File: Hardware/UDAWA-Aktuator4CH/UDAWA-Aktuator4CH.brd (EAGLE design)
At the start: 100 x 80 mm, 23 parts

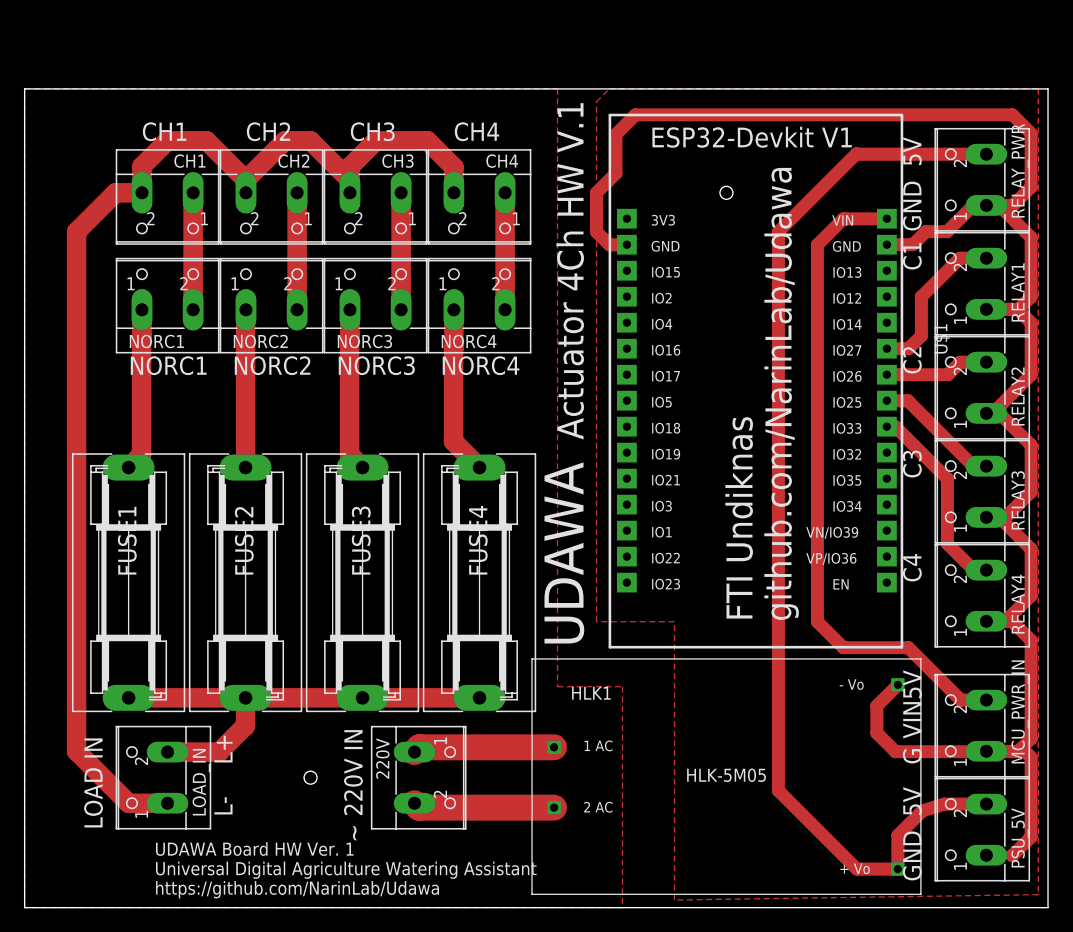
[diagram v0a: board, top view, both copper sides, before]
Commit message: Revisi mirroring. Board tidak mirror. Silkscreen mirror.
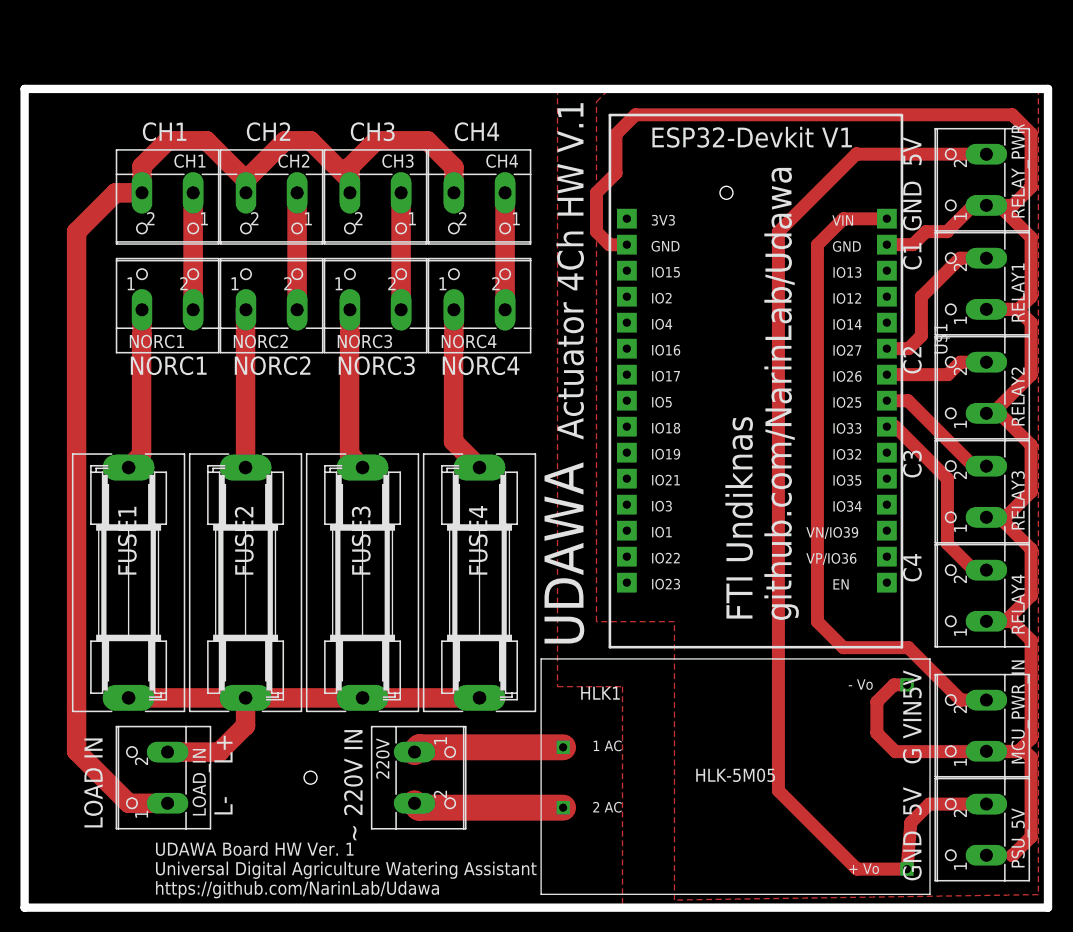
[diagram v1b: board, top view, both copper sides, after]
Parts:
- moved HLK1 0.89 mm to (69.5, 12.7)
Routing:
- net GND: track 192.8 -> 193.9 mm
- net AC2: track 13.8 -> 14.7 mm
- net AC1: track 13.8 -> 14.7 mm
- net 5V: track 106.0 -> 106.5 mm
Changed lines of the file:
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@@
 <grid distance="50" unitdist="mil" unit="mil" style="lines" multiple="1" display="no" altdistance="5" altunitdist="mil" altunit="mil"/>
 <layers>
-<layer number="1" name="Top" color="4" fill="1" visible="no" active="yes"/>
+<layer number="1" name="Top" color="4" fill="1" visible="yes" active="yes"/>
 <layer number="16" name="Bottom" color="1" fill="1" visible="yes" active="yes"/>
 <layer number="17" name="Pads" color="2" fill="1" visible="yes" active="yes"/>
@@
 <board>
 <plain>
-<wire x1="0" y1="0" x2="100" y2="0" width="0" layer="20"/>
-<wire x1="100" y1="0" x2="100" y2="80" width="0" layer="20"/>
-<wire x1="100" y1="80" x2="0" y2="80" width="0" layer="20"/>
-<wire x1="0" y1="80" x2="0" y2="0" width="0" layer="20"/>
+<wire x1="0" y1="0" x2="100" y2="0" width="0.8128" layer="20"/>
+<wire x1="100" y1="0" x2="100" y2="80" width="0.8128" layer="20"/>
+<wire x1="100" y1="80" x2="0" y2="80" width="0.8128" layer="20"/>
+<wire x1="0" y1="80" x2="0" y2="0" width="0.8128" layer="20"/>
 <text x="12.7" y="1.27" size="1.27" layer="21">UDAWA Board HW Ver. 1
 Universal Digital Agriculture Watering Assistant
@@
 <attribute name="VALUE" x="43.561" y="36.322" size="1.778" layer="27" ratio="10" rot="R270"/>
 </element>
-<element name="HLK1" library="HLK-5M05" package="HLK-5M05" value="5VDC/5W" x="68.58" y="12.7" smashed="yes">
-<attribute name="NAME" x="53.34" y="20.32" size="1.27" layer="21"/>
-<attribute name="SIZE" value="23x38(mm)" x="68.58" y="12.7" size="1.778" layer="27" display="off"/>
-<attribute name="VALUE" value="5VDC/5W" x="68.58" y="12.7" size="1.778" layer="27" display="off"/>
+<element name="HLK1" library="HLK-5M05" package="HLK-5M05" value="5VDC/5W" x="69.469" y="12.7" smashed="yes">
+<attribute name="NAME" x="54.229" y="20.32" size="1.27" layer="21"/>
+<attribute name="SIZE" value="23x38(mm)" x="69.469" y="12.7" size="1.778" layer="27" display="off"/>
+<attribute name="VALUE" value="5VDC/5W" x="69.469" y="12.7" size="1.778" layer="27" display="off"/>
 </element>
 <element name="U$1" library="ESP32-DEVKITV1" package="ESP32-DEVKITV1" value="ESP32DEVKITV1" x="71.12" y="50.8" smashed="yes" rot="R270">
@@
 <wire x1="98.349" y1="6.909" x2="98.349" y2="14.681" width="1.27" layer="1"/>
 <contactref element="HLK1" pad="3"/>
-<wire x1="85.33" y1="21.77" x2="83.28" y2="19.72" width="1.27" layer="1"/>
-<wire x1="83.28" y1="19.72" x2="83.28" y2="17.05" width="1.27" layer="1"/>
+<wire x1="86.219" y1="21.77" x2="84.949" y2="21.77" width="1.27" layer="1"/>
+<wire x1="84.949" y1="21.77" x2="83.28" y2="20.101" width="1.27" layer="1"/>
+<wire x1="83.28" y1="20.101" x2="83.28" y2="17.05" width="1.27" layer="1"/>
 <contactref element="PSU_5V" pad="1"/>
 </signal>
@@
 <wire x1="73.66" y1="11.43" x2="73.66" y2="66.04" width="1.27" layer="1"/>
 <contactref element="HLK1" pad="4"/>
-<wire x1="85.33" y1="3.77" x2="81.32" y2="3.77" width="1.27" layer="1"/>
+<wire x1="86.219" y1="3.77" x2="81.32" y2="3.77" width="1.27" layer="1"/>
 <wire x1="81.32" y1="3.77" x2="73.66" y2="11.43" width="1.27" layer="1"/>
 <contactref element="PSU_5V" pad="2"/>
-<wire x1="87.738996875" y1="9.458996875" x2="89.875359375" y2="10.12" width="1.27" layer="1"/>
-<wire x1="89.875359375" y1="10.12" x2="93.98" y2="10.12" width="1.27" layer="1"/>
-<wire x1="85.33" y1="3.77" x2="85.33" y2="7.05" width="1.27" layer="1"/>
-<wire x1="85.33" y1="7.05" x2="87.738996875" y2="9.458996875" width="1.27" layer="1"/>
+<wire x1="88.4" y1="10.12" x2="93.98" y2="10.12" width="1.27" layer="1"/>
+<wire x1="86.219" y1="3.77" x2="86.6" y2="8.32" width="1.27" layer="1"/>
+<wire x1="86.6" y1="8.32" x2="88.4" y2="10.12" width="1.27" layer="1"/>
 </signal>
 <signal name="AC1">
@@
 <contactref element="220V" pad="2"/>
 <wire x1="38.1" y1="10.2" x2="38.53" y2="9.77" width="2.54" layer="1"/>
-<wire x1="38.53" y1="9.77" x2="51.73" y2="9.77" width="2.54" layer="1"/>
+<wire x1="38.53" y1="9.77" x2="52.619" y2="9.77" width="2.54" layer="1"/>
 </signal>
 <signal name="AC2">
@@
 <contactref element="220V" pad="1"/>
 <wire x1="38.1" y1="15.2" x2="38.57" y2="15.67" width="2.54" layer="1"/>
-<wire x1="38.57" y1="15.67" x2="51.73" y2="15.67" width="2.54" layer="1"/>
+<wire x1="38.57" y1="15.67" x2="52.619" y2="15.67" width="2.54" layer="1"/>
 </signal>
 <signal name="C4">
